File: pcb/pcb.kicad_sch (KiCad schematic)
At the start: 51 parts, among them J1 MJ-4PP-9, SW1 SW_PUSH, SW10 SW_PUSH, SW11 SW_PUSH, SW12 SW_PUSH, SW13 SW_PUSH, SW14 SW_PUSH, SW15 SW_PUSH, SW16 SW_PUSH, SW17 SW_PUSH, SW18 SW_PUSH, SW2 SW_PUSH, SW3 SW_PUSH, SW4 SW_PUSH, SW5 SW_PUSH, SW6 SW_PUSH, SW7 SW_PUSH, SW8 SW_PUSH, SW9 SW_PUSH, U1 xiao-ble, U2 xiao-ble

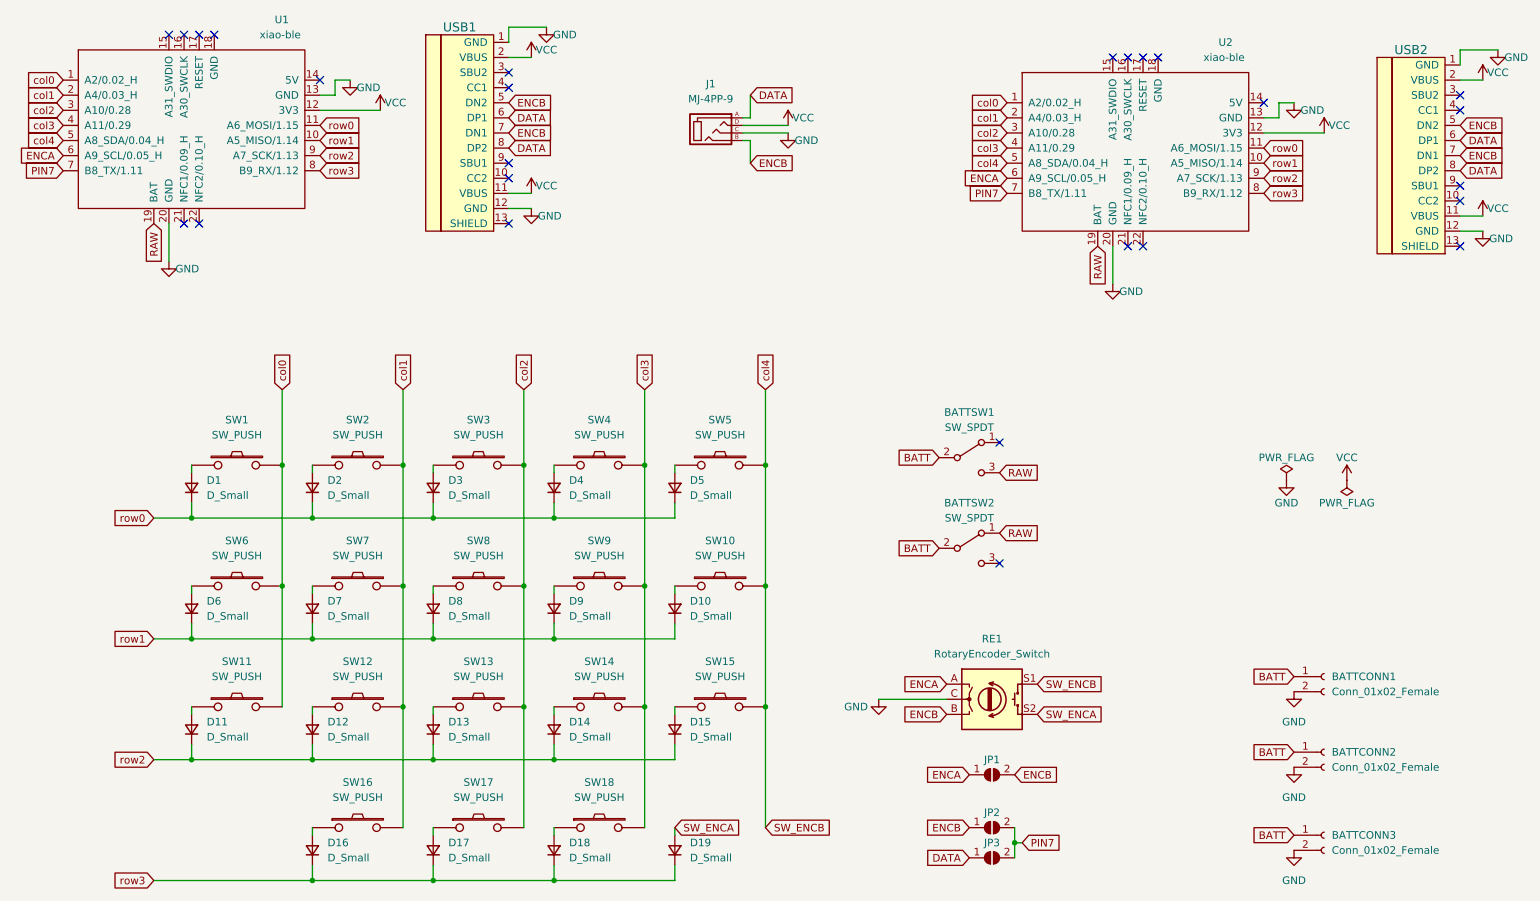
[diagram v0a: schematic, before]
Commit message: migrate to my own library
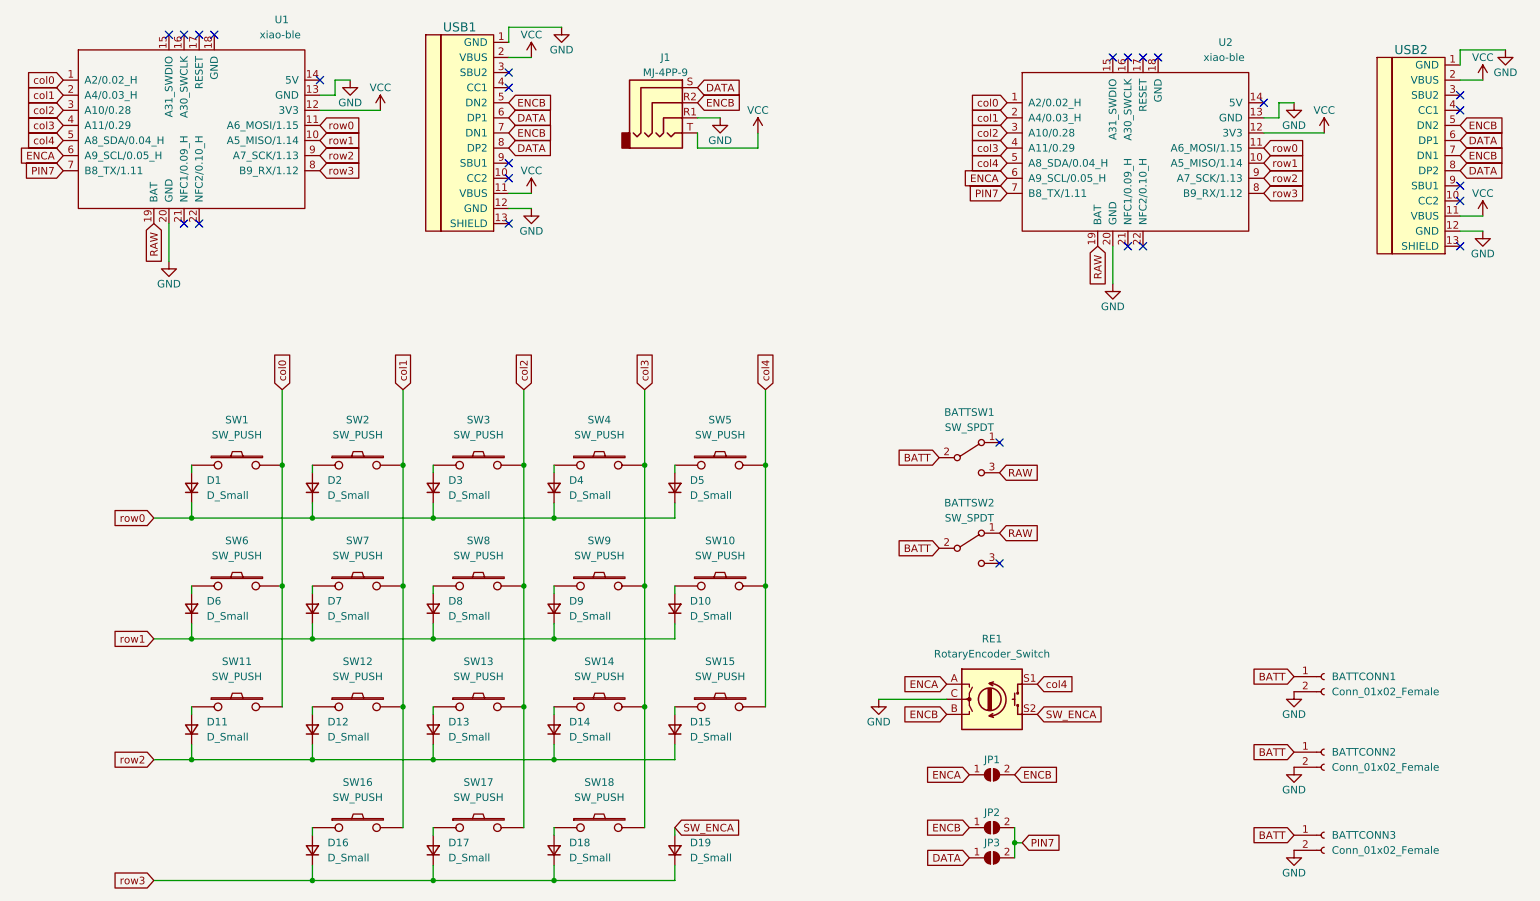
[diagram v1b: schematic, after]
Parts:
- BATTCONN1, BATTCONN2, BATTCONN3: footprint picachoc:JST_PH_S2B-PH-K_1x02_P2.00mm -> zzkeeb:Connector_JST-1x02-2.00mm
- BATTSW1, BATTSW2: footprint Button_Switch_SMD:SW_SPDT_PCM12 -> zzkeeb:Switch_SPDT-PCM12
- D1, D10, D11, D12, D13, D14, D15, D16, D17, D18, D19, D2, D3, D4, D5, D6, D7, D8, D9: footprint picachoc:D3_SMD -> zzkeeb:Diode_1N4148-SOD123-reversible
- J1: footprint picachoc:MJ-4PP-9 -> zzkeeb:Connector_TRRS-reversible; symbol kbd:MJ-4PP-9 -> Connector:AudioJack4
- RE1: footprint picachoc:RotaryEncoder_EC11 -> zzkeeb:RotaryEncoder_EC11-reversible
- SW1, SW10, SW11, SW12, SW13, SW14, SW15, SW16, SW17, SW18, SW2, SW3, SW4, SW5, SW6, SW7, SW8, SW9: footprint picachoc:Kailh-PG1350-1u -> zzkeeb:Switch_ChocV1-reversible; symbol kbd:SW_PUSH -> zzkeeb:Switch
- U1, U2: footprint picachoc:xiao-ble-smd -> zzkeeb:MCU_xiao-ble-smd; symbol kleeb-mcu:xiao-ble -> zzkeeb:MCU_xiao-ble
- USB1, USB2: footprint picachoc:HRO-TYPE-C-31-M-12-data -> zzkeeb:Connector_HRO-TYPE-C-31-M-12-data; symbol typec:HRO-TYPE-C-31-M-12 -> zzkeeb:Connector_HRO-TYPE-C-31-M-12
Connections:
- net DATA: now also J1.S; no longer J1.A
- net ENCB: now also J1.R2; no longer J1.B
- net GND: now also J1.R1; no longer J1.C
- net VCC: now also J1.T; no longer J1.D
- net SW_ENCB renamed col4
